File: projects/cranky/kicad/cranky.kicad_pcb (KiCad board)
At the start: 2 copper layers, 50 x 50 mm, 51 parts, among them CON1 USB-MINI-B, P1 ISP, P2 CONN_01X04, P3 CONN_01X04, P4 CONN_01X04, P5 CONN_01X04, Q1 2N7002P, Q2 2N7002P, Q3 ISL9V3040D3ST, Q4 ISL9V3040D3ST, Q5 VND5N07, Q6 VND5N07, SW1 SW_PUSH_SMALL, SW2 SW_PUSH_SMALL, U1 ATMEGA32U4-A, U2 LTV-826S, U3 LM7805CT, X1 16MHz

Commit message: routing new cranky board
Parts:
- removed P3, P4, P5: CONN_01X04, SCREW_TERMINAL_4
- removed WJ10: VAL**, WJ10
- added C17: 0.1, Capacitors_SMD:C_0603, F.Cu at (76.8, 86.4)
- added C18: 1n, Capacitors_SMD:C_0603, F.Cu at (88.9, 84.5)
- added C19: .001, Capacitors_SMD:C_0603, F.Cu at (88.9, 80.6)
- added C20: .001, Capacitors_SMD:C_0603, F.Cu at (88.9, 82.5)
- added C21: 220n, Capacitors_SMD:C_0603, F.Cu at (82.5, 84.5)
- added C22: 1, Capacitors_SMD:C_0603, F.Cu at (82.5, 80.6)
- added C23: 1, Capacitors_SMD:C_0603, F.Cu at (82.5, 82.5)
- added C24: 1, Capacitors_SMD:C_0603, F.Cu at (82.5, 78.7)
- added D3: Led_Small, LEDs:LED-0603, F.Cu at (62.9, 73.0)
- added D4: Led_Small, LEDs:LED-0603, F.Cu at (87.0, 73.0)
- added R14: 4.7k, Resistors_SMD:R_0603, F.Cu at (54.6, 76.2)
- added R15: 4.7k, Resistors_SMD:R_0603, F.Cu at (51.4, 76.2)
- added R16: 1M, Resistors_SMD:R_0603, F.Cu at (88.9, 78.7)
- added R17: 50k, Resistors_SMD:R_0603, F.Cu at (59.1, 88.3)
- added R18: 1k, Resistors_SMD:R_0603, F.Cu at (85.7, 84.5)
- added R19: 2.2k, Resistors_SMD:R_0603, F.Cu at (85.7, 80.6)
- added R20: 2.2k, Resistors_SMD:R_0603, F.Cu at (85.7, 82.5)
- added R21: 1k, Resistors_SMD:R_0603, F.Cu at (85.7, 78.7)
- added R22: 10k, Resistors_SMD:R_0603, F.Cu at (59.1, 86.4)
- added R23: 1k, Resistors_SMD:R_0603, F.Cu at (62.9, 71.1)
- added R24: 1k, Resistors_SMD:R_0603, F.Cu at (87.0, 71.1)
- added WJ20: VAL**, DigitalCave:WJ20, B.Cu at (69.2, 81.3)
- C1, C2, C6: value 220nF -> .22; footprint SM0603_VALUE -> Capacitors_SMD:C_0603
- C10, C7: value 20pF -> 20p; footprint SM0603_VALUE -> Capacitors_SMD:C_0603
- C11, C9: value 33uF -> 33; footprint C1V5 -> Discret:C1V5H; moved to B.Cu
- C12, C13, C14, C15: value 0.1u -> 0.1; footprint SM0603_VALUE -> Capacitors_SMD:C_0603
- C16: value 100n -> 1; footprint custom:SM0603_VALUE -> Capacitors_SMD:C_0603
- C3, C5: value 1nF -> .001; footprint SM0603_VALUE -> Capacitors_SMD:C_0603
- C4: value 1nF -> 1n; footprint SM0603_VALUE -> Capacitors_SMD:C_0603
- C8: footprint SM0603_VALUE -> Capacitors_SMD:C_0603
- CON1: footprint USB_MINI_B_fixed -> DigitalCave:USB_MINI_B_fixed
- D1, D2: footprint SOT23 -> Diodes_SMD:SOD-523
- F1: footprint FUSE_TE5 -> Fuse_Holders_and_Fuses:Fuse_TE5_Littlefuse-395Series; moved to B.Cu
- P1: footprint ISP_EDGE -> DigitalCave:ISP_EDGE
- P2: value CONN_01X04 -> AMP794106; footprint SCREW_TERMINAL_4 -> DigitalCave:AMP794106; moved to B.Cu
- Q1, Q2: footprint SOT23 -> TO_SOT_Packages_SMD:SOT-23
- Q3, Q4, Q5, Q6, U3: footprint DPAK2 -> TO_SOT_Packages_SMD:TO-252-2Lead
- R1, R10, R11, R12, R13, R2, R3, R4, R5, R6, R7, R8, R9: footprint SM0603_VALUE -> Resistors_SMD:R_0603
- SW1, SW2: footprint SW_6x3 -> DigitalCave:SW_6x3; moved to B.Cu
- U1: footprint TQFP44 -> Housings_QFP:TQFP-44_10x10mm_Pitch0.8mm
- U2: footprint SO8E -> Housings_SOIC:SOIC-8_3.9x4.9mm_Pitch1.27mm
- X1: footprint crystal_smd_2.5x2 -> DigitalCave:CRYSTAL_SMD_2.5x2
- moved CON1 43.1 mm to (87.6, 116.8), turned to 90 degrees
- moved R8 41.6 mm to (50.2, 115.6)
- moved Q2 39.9 mm to (50.8, 112.4), turned to 270 degrees
- moved P2 36.1 mm to (70.0, 107.3), turned to 180 degrees
- moved C2 35.7 mm to (54.6, 88.3), turned to 0 degrees
- moved C16 35.6 mm to (62.9, 88.3), turned to 180 degrees
- moved C5 35.5 mm to (54.6, 84.5), turned to 180 degrees
- moved R2 35.3 mm to (54.6, 86.4), turned to 180 degrees
- moved C1 35.0 mm to (51.4, 88.3), turned to 180 degrees
- moved C4 34.9 mm to (51.4, 84.5)
- moved R1 34.7 mm to (51.4, 86.4), turned to 0 degrees
- moved R7 33.5 mm to (54.6, 115.6)
- moved U2 33.4 mm to (53.3, 80.0)
- moved Q1 31.5 mm to (55.2, 112.4), turned to 270 degrees
- moved C9 29.2 mm to (51.4, 72.4), turned to 180 degrees
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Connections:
- net /X1 renamed /X+
- net /X2 renamed /X-
- C11 pad 1: VCC -> Net-(C11-Pad1)
- C13 pad 1: VCC -> DGND
- C13 pad 2: DGND -> VCC
- C15 pad 1: VCC -> DGND
- C15 pad 2: DGND -> VCC
- C16 pad 1: DGND -> Net-(C16-Pad1)
- C16 pad 2: Net-(C16-Pad2) -> DGND
- C8 pad 1: DGND -> /UCAP
- C8 pad 2: /UCAP -> DGND
- C9 pad 1: Net-(C9-Pad1) -> /IGR
- CON1 pad 1: Net-(CON1-Pad1) -> /VBUS
- CON1 pad 2: Net-(CON1-Pad2) -> /UDM
- CON1 pad 3: Net-(CON1-Pad3) -> /UDP
- CON1 pad 4: Net-(CON1-Pad4) -> (no net)
- CON1 pad 5: Net-(CON1-Pad5) -> DGND
- CON1 pad 6: Net-(CON1-Pad6) -> DGND
- CON1 pad 7: Net-(CON1-Pad7) -> DGND
- CON1 pad 8: Net-(CON1-Pad8) -> DGND
- CON1 pad 9: Net-(CON1-Pad9) -> DGND
- D1 pad 1: GNDPWR -> DGND
- D2 pad 1: GNDPWR -> DGND
- F1 pad 1: Net-(C9-Pad1) -> Net-(C11-Pad1)
- F1 pad 2: /IGR -> VCC
- P2 pad 1: GNDPWR -> /IGR
- P2 pad 2: GNDPWR -> DGND
- P2 pad 3: GNDPWR -> VCC
- P2 pad 4: GNDPWR -> DGND
- Q3 pad 3: GNDPWR -> DGND
- Q4 pad 3: GNDPWR -> DGND
- Q5 pad S: GNDPWR -> DGND
- Q6 pad S: GNDPWR -> DGND
- R12 pad 2: /PD4 -> /PD7
- R13 pad 2: /PD5 -> /PD6
- U1 pad 1: Net-(U1-Pad1) -> (no net)
- U1 pad 12: Net-(U1-Pad12) -> (no net)
- U1 pad 18: Net-(U1-Pad18) -> (no net)
- U1 pad 19: Net-(U1-Pad19) -> (no net)
- U1 pad 2: /UVCC -> VCC
- U1 pad 22: /PD5 -> (no net)
- U1 pad 25: /PD4 -> (no net)
- U1 pad 26: Net-(U1-Pad26) -> /PD6
- U1 pad 27: Net-(U1-Pad27) -> /PD7
- U1 pad 30: Net-(U1-Pad30) -> (no net)
- U1 pad 36: Net-(U1-Pad36) -> /ADC7
- U1 pad 37: Net-(U1-Pad37) -> /ADC6
- U1 pad 38: Net-(U1-Pad38) -> /ADC5
- U1 pad 39: Net-(U1-Pad39) -> /ADC4
- U1 pad 40: Net-(U1-Pad40) -> /ADC1
- U1 pad 42: Net-(C16-Pad2) -> Net-(C16-Pad1)
- U1 pad 5: /UGND -> DGND
- U2 pad 6: /INT3 -> /INT2
- U2 pad 8: /INT2 -> /INT3
- U3 pad 1: Net-(C9-Pad1) -> /IGR
- U3 pad 3: VCC -> Net-(C11-Pad1)
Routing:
- net GNDPWR: track 125.8 -> 0.00 mm, vias 28 -> 0
- net DGND: track 60.2 -> 184.2 mm, vias 11 -> 27
- net /PB4: track 80.5 -> 13.0 mm
- net /VBUS: track 0.00 -> 57.4 mm, vias 0 -> 2
- net /UDM: track 0.00 -> 43.4 mm
- net /UDP: track 2.39 -> 45.4 mm
- net /PC6: track 12.3 -> 55.0 mm
- net /IGR: track 21.9 -> 62.4 mm, vias 0 -> 1
- net /CAT: track 0.00 -> 40.0 mm, vias 0 -> 1
- net /O2: track 0.00 -> 38.7 mm, vias 0 -> 1
- net /PB5: track 48.5 -> 11.8 mm
- net /MAT: track 0.00 -> 35.5 mm, vias 0 -> 1
- net /IGNB: track 52.0 -> 16.6 mm, vias 10 -> 0
- net /PC7: track 13.0 -> 48.2 mm
- net /PD5: track 31.4 -> 0.00 mm, vias 2 -> 0
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- removed copper zone on B.Cu, net /IGNA
- removed copper zone on F.Cu, net /IGNA
- removed copper zone on B.Cu, net /IGNB
- removed copper zone on F.Cu, net /IGNB
- removed copper zone on F.Cu, net DGND
- removed copper zone on B.Cu, net GNDPWR
- removed copper zone on F.Cu, net GNDPWR
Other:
- net class Default: clearance 0.2032 -> 0.1778; trace_width 0.254 -> 0.1778; via_dia 0.889 -> 0.6858; via_drill 0.635 -> 0.3556
- rule trace_clearance: 0.2032 -> 0.1778
- rule trace_min: 0.254 -> 0.1778
- rule via_min_drill: 0.508 -> 0.3556
- rule via_min_size: 0.889 -> 0.6858
- board text added: "+"
- board text added: "CAT"
- board text added: "Cranky ECM 1.0"
- board text added: "IGR"
- board text added: "MAP"
- board text added: "MAT"
- board text added: "O2"
- board text added: "VCC"
- board text removed: "5V"
- board text removed: "Cranky v1.0"
- board text removed: "GND"
- board text removed: "IGN"
- board text removed: "INJA"
- board text removed: "INJB"
- board text removed: "PGND"

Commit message: re-adding buttons, working towards continuous gnd plane
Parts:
- moved D3 22.9 mm to (85.7, 73.0)
- moved R23 22.9 mm to (85.7, 71.1)
- moved SW2 20.1 mm to (63.5, 82.5), turned to 90 degrees
- moved WJ20 17.5 mm to (81.3, 94.0)
- moved SW1 12.8 mm to (74.3, 78.1)
- moved D4 1.91 mm to (88.9, 73.0)
- moved R24 1.91 mm to (88.9, 71.1)
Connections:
- D1 pad 1: DGND -> /IGNA_GND
- D2 pad 1: DGND -> /IGNB_GND
- P2 pad 10: DGND -> /INJB_GND
- P2 pad 16: DGND -> /IGNA_GND
- P2 pad 4: DGND -> /IGNB_GND
- P2 pad 8: DGND -> /INJA_GND
- Q3 pad 3: DGND -> /IGNA_GND
- Q4 pad 3: DGND -> /IGNB_GND
- Q5 pad S: DGND -> /INJA_GND
- Q6 pad S: DGND -> /INJB_GND
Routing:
- net DGND: track 184.2 -> 134.7 mm, vias 27 -> 26
- net VCC: track 101.0 -> 116.9 mm, vias 1 -> 3
- net /IGNA_GND: track 0.00 -> 7.52 mm
- net /IGNB_GND: track 0.00 -> 7.20 mm
- net //RST: track 18.7 -> 24.1 mm
- net /INJA_GND: track 0.00 -> 4.17 mm
- net /INJB_GND: track 0.00 -> 4.13 mm
- net //HWB: track 7.65 -> 10.9 mm, vias 0 -> 1
- net Net-(D4-Pad2): track 19.6 -> 22.6 mm
- net Net-(Q3-Pad1): track 29.6 -> 32.0 mm
- net /CAM: track 29.8 -> 31.3 mm
- net /ADC7: track 11.4 -> 12.4 mm
- net /X-: track 7.62 -> 8.57 mm
- net /X+: track 4.71 -> 5.34 mm
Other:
- board text added: "HWB"
- board text added: "IND"
- board text added: "PWR"
- board text added: "RESET"

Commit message: another big overhaul (wyatt is evil)
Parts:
- C11, C9: value 33 -> .33; footprint Discret:C1V5H -> Capacitors_SMD:C_0603; moved to F.Cu
- F1: value 2A -> 500mA; footprint Fuse_Holders_and_Fuses:Fuse_TE5_Littlefuse-395Series -> Resistors_SMD:R_0603; moved to F.Cu
- moved U3 24.5 mm to (57.8, 74.9), turned to 90 degrees
- moved F1 16.2 mm to (49.5, 80.6)
- moved C16 9.52 mm to (72.4, 88.3), turned to 0 degrees
- moved C9 8.64 mm to (59.7, 74.9), turned to 0 degrees
- moved C1 7.24 mm to (55.9, 94.0)
- moved C2 7.24 mm to (59.1, 94.0)
- moved C4 7.24 mm to (55.9, 90.2)
- moved C5 7.24 mm to (59.1, 90.2)
- moved R1 7.24 mm to (55.9, 92.1)
- moved R2 7.24 mm to (59.1, 92.1)
- moved R15 6.48 mm to (52.7, 82.5), turned to 180 degrees
- moved R22 5.85 mm to (62.9, 90.8)
- moved R17 5.85 mm to (62.9, 92.7)
- moved U2 5.85 mm to (57.8, 83.8), turned to 90 degrees
- moved R9 5.39 mm to (62.9, 88.3)
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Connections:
- C11 pad 1: Net-(C11-Pad1) -> VCC
- C9 pad 1: /IGR -> Net-(C9-Pad1)
- F1 pad 1: Net-(C11-Pad1) -> /IGR
- F1 pad 2: VCC -> Net-(C9-Pad1)
- R7 pad 1: /PC6 -> /PC7
- R8 pad 1: /PC7 -> /PC6
- U3 pad 1: /IGR -> Net-(C9-Pad1)
- U3 pad 3: Net-(C11-Pad1) -> VCC
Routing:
- net Net-(C11-Pad1): track 29.9 -> 0.00 mm
- net /IGR: track 62.4 -> 37.1 mm, vias 1 -> 2
- net DGND: track 134.7 -> 119.7 mm, vias 26 -> 48
- net /CRNK: track 31.1 -> 16.5 mm, vias 1 -> 0
- net Net-(C9-Pad1): track 0.00 -> 13.0 mm
- net VCC: track 116.9 -> 129.5 mm, vias 3 -> 4
- net /CAM: track 31.3 -> 18.7 mm, vias 1 -> 0
- net Net-(C16-Pad1): track 11.3 -> 2.17 mm, vias 2 -> 0
- net //HWB: track 10.9 -> 6.87 mm
- net /ADC7: track 12.4 -> 8.63 mm, vias 2 -> 0
- net Net-(C4-Pad1): track 9.36 -> 5.87 mm, vias 2 -> 0
- net /PC6: track 55.0 -> 51.6 mm
- net Net-(C5-Pad1): track 9.25 -> 6.13 mm
- net /INT3: track 15.4 -> 18.1 mm
- net /INT2: track 25.3 -> 23.7 mm
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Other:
- board text removed: "+"

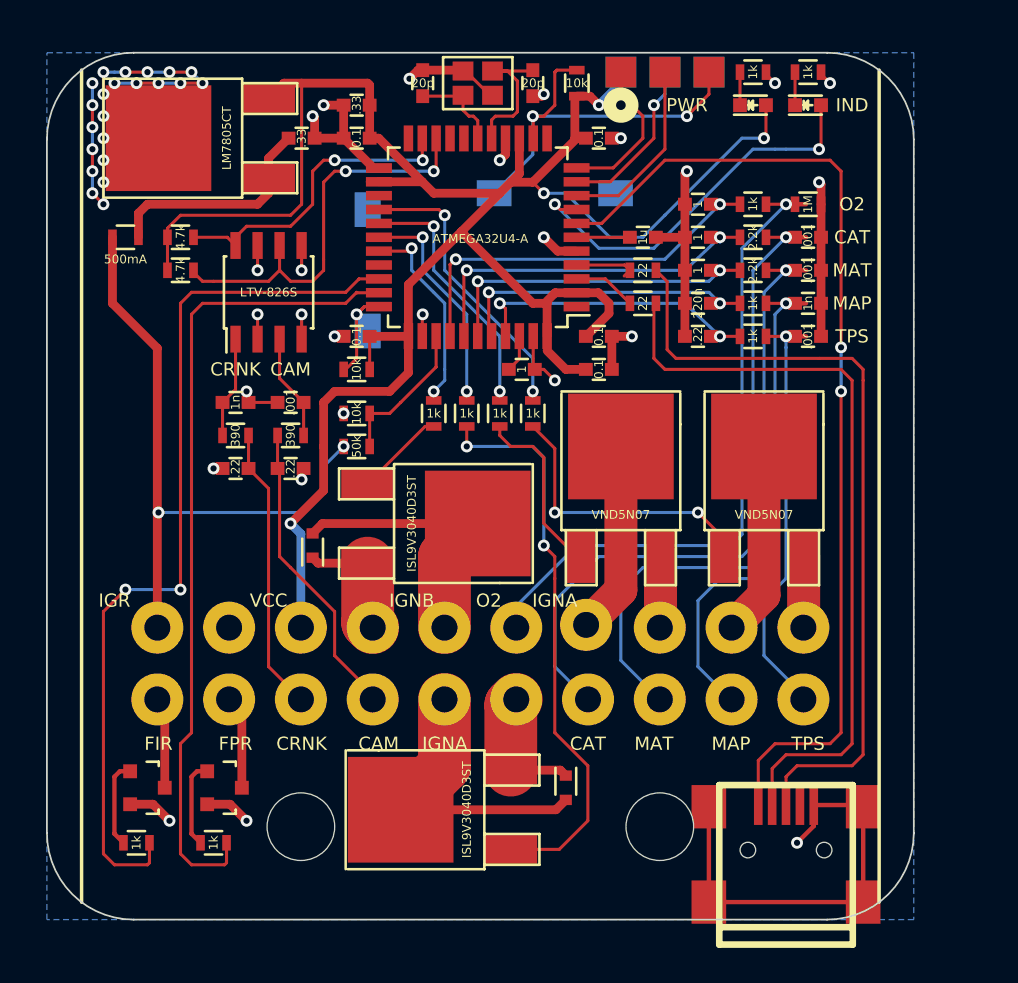
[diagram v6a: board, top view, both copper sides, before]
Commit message: adding heat sink vias, moving buttons
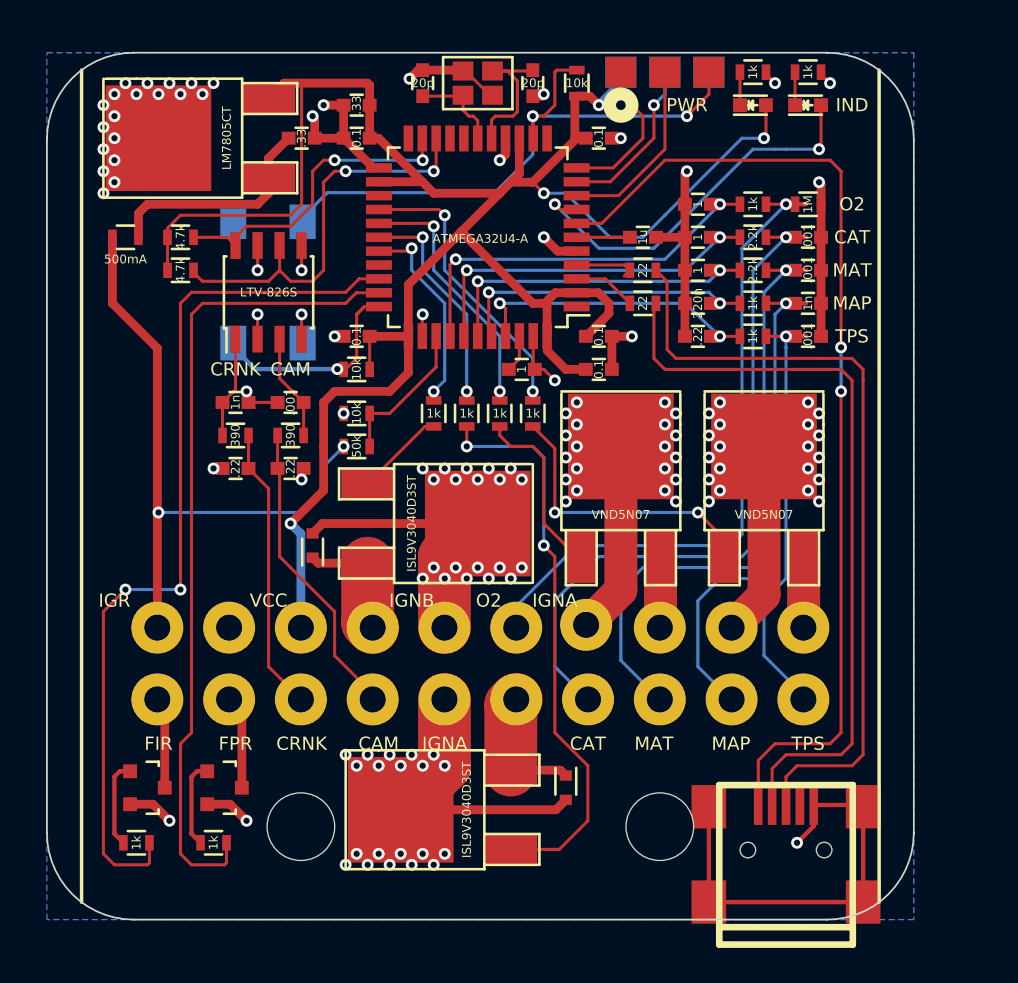
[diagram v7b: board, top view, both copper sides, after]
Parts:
- moved SW1 15.4 mm to (59.8, 83.2), turned to 90 degrees
- moved SW2 7.78 mm to (55.8, 83.2)
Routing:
- net /IGNA: track 17.2 -> 49.5 mm, vias 0 -> 20
- net /IGNB: track 16.6 -> 48.9 mm, vias 0 -> 20
- net /INJA: track 11.1 -> 43.4 mm, vias 0 -> 20
- net /INJB: track 11.2 -> 43.6 mm, vias 0 -> 20
- net //RST: track 24.1 -> 36.0 mm
- net DGND: track 119.7 -> 110.2 mm, vias 48 -> 45
- net //HWB: track 6.87 -> 12.8 mm

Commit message: moving leds to the front of the board
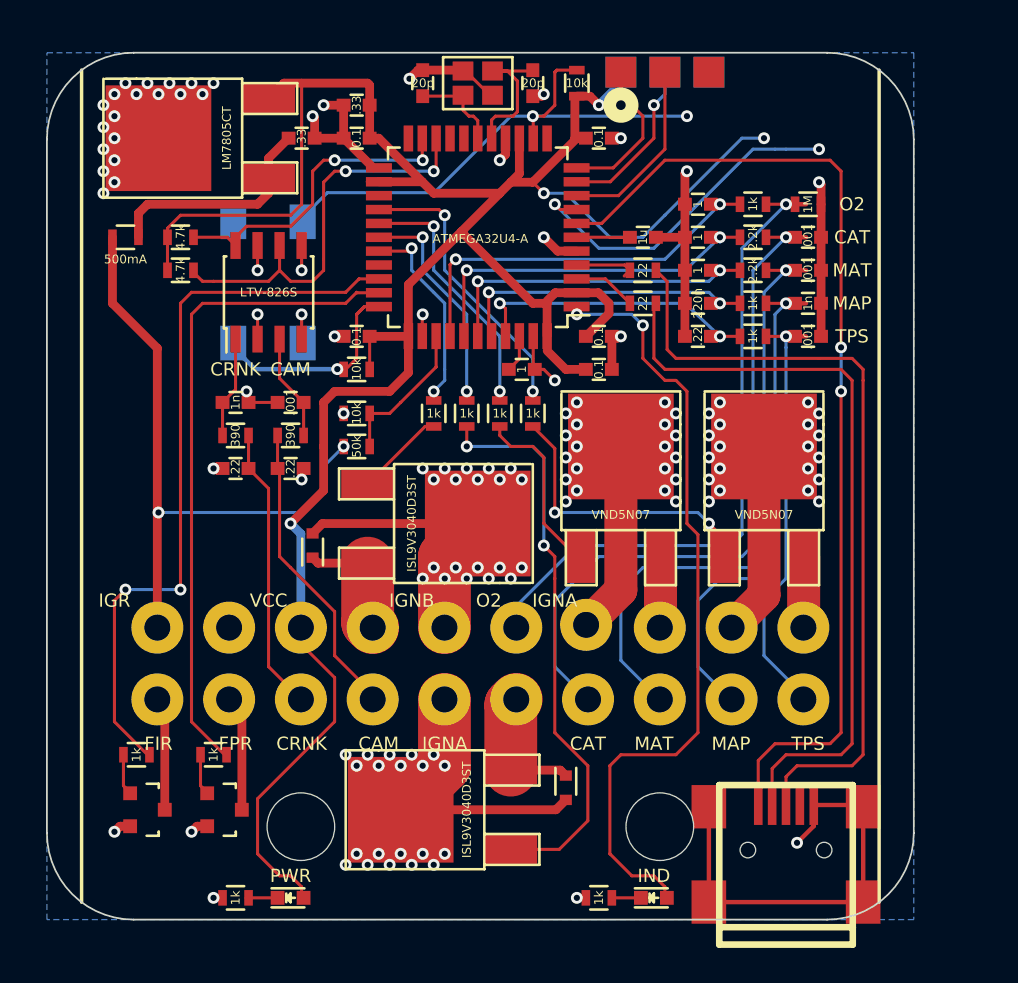
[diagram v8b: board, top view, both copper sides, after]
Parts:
- moved R23 56.2 mm to (55.9, 118.7), turned to 180 degrees
- moved D3 52.9 mm to (59.1, 118.7)
- moved R24 49.1 mm to (76.8, 118.7), turned to 0 degrees
- moved D4 46.6 mm to (80.0, 118.7)
- moved WJ20 23.1 mm to (69.2, 74.3)
- moved R7 5.08 mm to (54.6, 110.5)
- moved R8 5.08 mm to (50.2, 110.5)
- moved Q1 1.27 mm to (55.2, 113.7)
- moved Q2 1.27 mm to (50.8, 113.7)
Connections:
- CON1 pad 4: (no net) -> Net-(CON1-Pad4)
- D4 pad 2: Net-(D4-Pad2) -> /LED
- U1 pad 1: (no net) -> /LED
- U1 pad 12: (no net) -> Net-(U1-Pad12)
- U1 pad 18: (no net) -> Net-(U1-Pad18)
- U1 pad 19: (no net) -> Net-(U1-Pad19)
- U1 pad 22: (no net) -> Net-(U1-Pad22)
- U1 pad 25: (no net) -> Net-(U1-Pad25)
- U1 pad 30: (no net) -> Net-(U1-Pad30)
- U1 pad 8: Net-(D4-Pad2) -> Net-(U1-Pad8)
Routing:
- net /LED: track 0.00 -> 45.7 mm, vias 0 -> 2
- net Net-(D4-Pad2): track 22.6 -> 0.00 mm, vias 2 -> 0
- net Net-(U1-Pad8): track 0.00 -> 20.2 mm, vias 0 -> 2
- net VCC: track 129.5 -> 147.9 mm
- net /PC7: track 46.8 -> 37.7 mm
- net /PC6: track 51.6 -> 42.4 mm
- net DGND: track 110.2 -> 105.7 mm
- net //RST: track 36.0 -> 31.6 mm
- net Net-(Q2-Pad1): track 5.06 -> 2.37 mm
- net Net-(Q1-Pad1): track 5.06 -> 2.37 mm
- net /FIR: track 5.27 -> 7.18 mm
- net Net-(Q6-PadG): track 16.9 -> 18.1 mm
- net /FPR: track 6.03 -> 6.87 mm
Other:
- board text added: "RST"
- board text removed: "RESET"
